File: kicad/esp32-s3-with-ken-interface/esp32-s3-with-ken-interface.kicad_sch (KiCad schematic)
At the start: 32 parts, among them J1 TYPE-C-31-M-12, Q1 UMH3N, SW1 TSC015A03526A, SW2 TSC015A03526A, SW3 TSC015A03526A, U1 CH340C, U2 AMS1117-3.3, U3 XDZ254-2-15-W-2.5-G1, U4 ESP32-S3-WROOM-1, U5 PM254-2-15-W-8.5

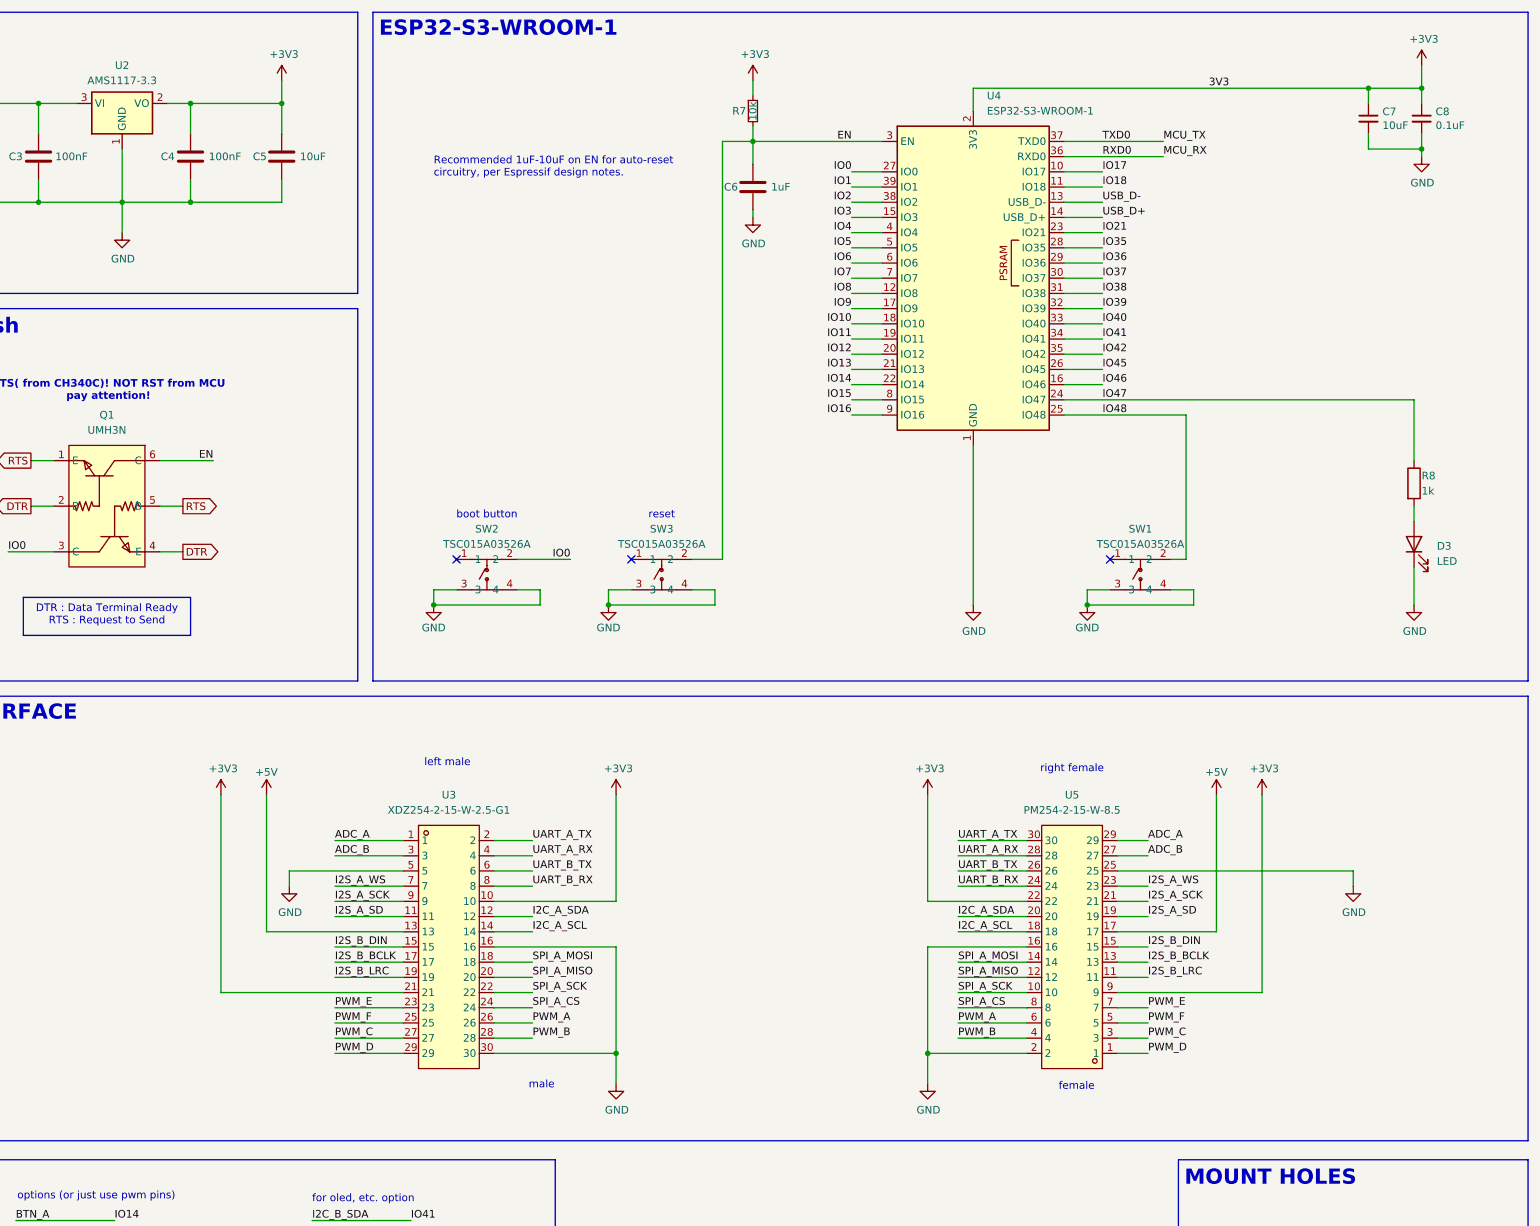
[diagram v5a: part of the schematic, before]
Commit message: add capacitor
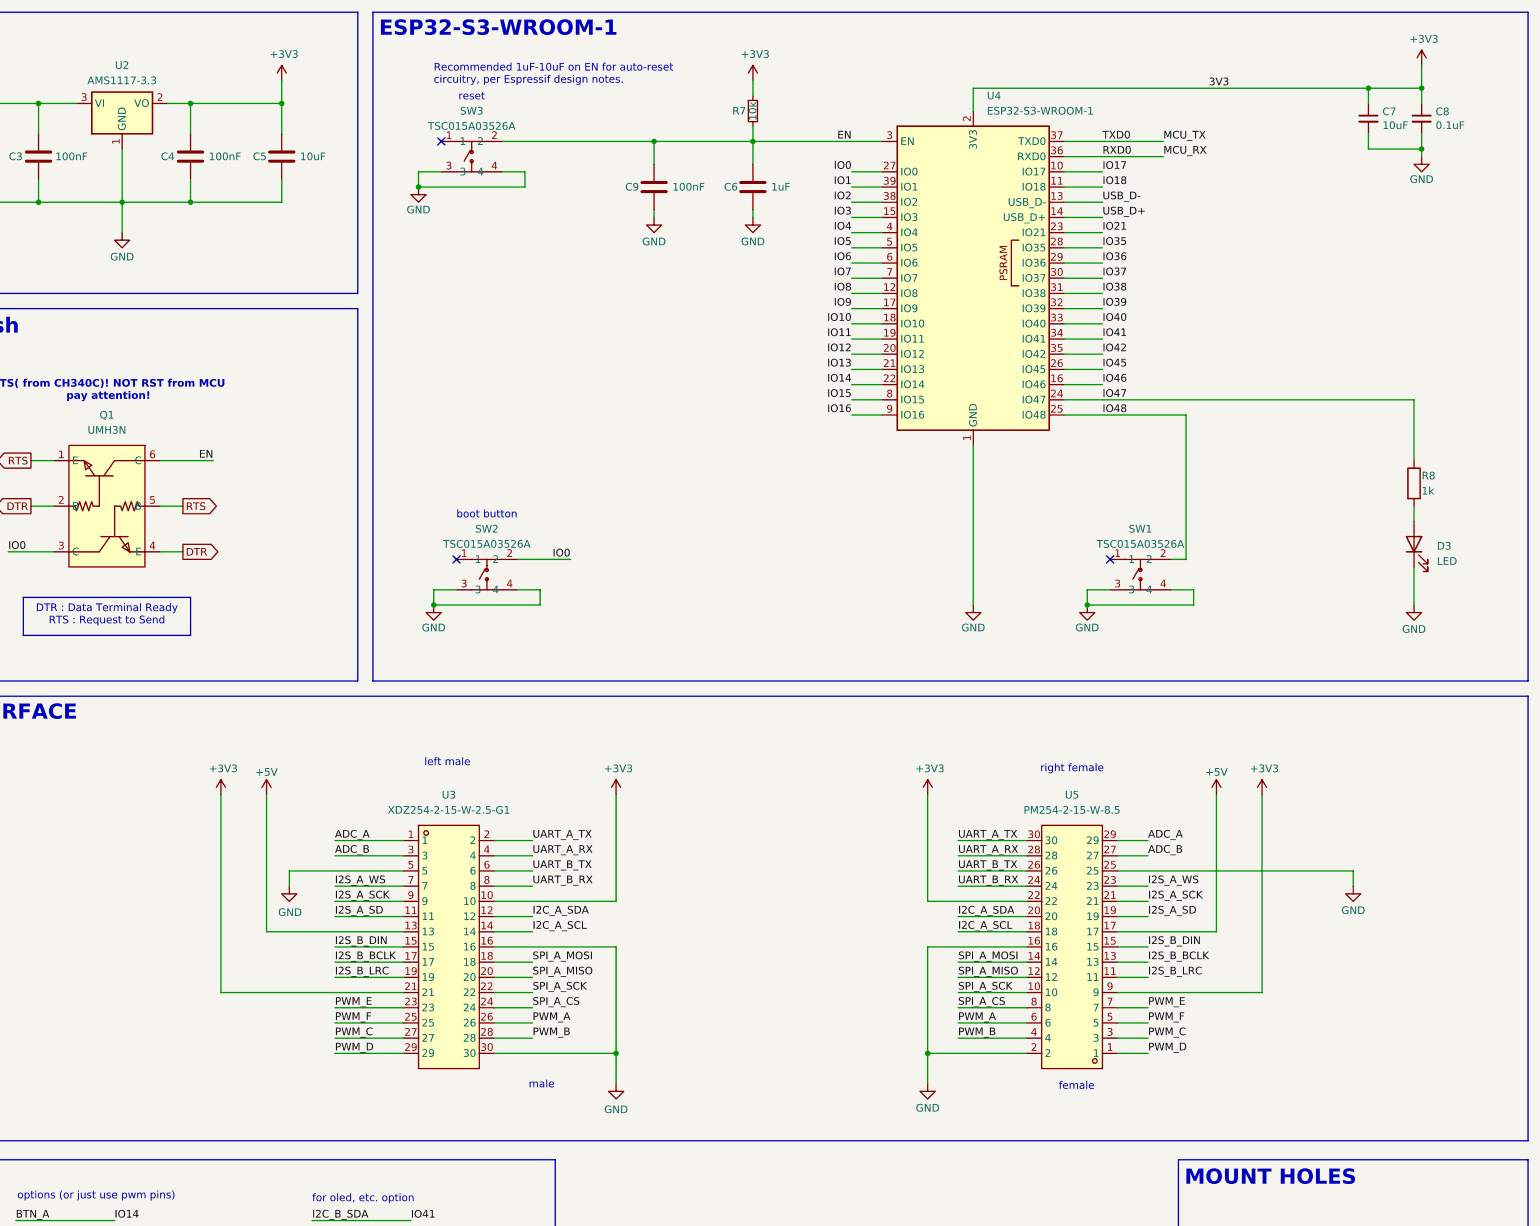
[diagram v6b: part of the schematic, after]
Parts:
- added C9: 100nF, Capacitor_SMD:C_0603_1608Metric_Pad1.08x0.95mm_HandSolder, symbol Device:C
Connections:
- net EN: now also C9.1
- net GND: now also C9.2
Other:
- moved on the sheet: SW3
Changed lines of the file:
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@@
 	(text "Recommended 1uF-10uF on EN for auto-reset\ncircuitry, per Espressif design notes."
 		(exclude_from_sim no)
-		(at 222.25 41.656 0)
+		(at 222.25 26.162 0)
 		(effects
 			(font
@@
 	(text "reset"
 		(exclude_from_sim no)
-		(at 260.35 98.044 0)
+		(at 228.6 28.194 0)
 		(effects
 			(font
@@
 	)
 	(junction
-		(at 251.46 113.03)
+		(at 219.71 43.18)
 		(diameter 0)
 		(color 0 0 0 0)
@@
 	)
 	(junction
+		(at 259.08 35.56)
+		(diameter 0)
+		(color 0 0 0 0)
+	)
+	(junction
 		(at 48.26 73.66)
 		(diameter 0)
@@
 	)
 	(no_connect
-		(at 255.27 105.41)
+		(at 223.52 35.56)
 	)
 	(no_connect
@@
 	(wire
 		(pts
-			(xy 269.24 113.03) (xy 251.46 113.03)
+			(xy 237.49 43.18) (xy 219.71 43.18)
+		)
+		(stroke
+			(width 0)
+			(type default)
+		)
+	)
+	(wire
+		(pts
+			(xy 259.08 46.99) (xy 259.08 48.26)
 		)
 		(stroke
@@
 	(wire
 		(pts
-			(xy 269.24 110.49) (xy 269.24 113.03)
+			(xy 237.49 40.64) (xy 237.49 43.18)
 		)
 		(stroke
@@
 	(wire
 		(pts
-			(xy 270.51 105.41) (xy 265.43 105.41)
+			(xy 233.68 35.56) (xy 259.08 35.56)
 		)
 		(stroke
@@
 	(wire
 		(pts
-			(xy 251.46 110.49) (xy 251.46 113.03)
+			(xy 219.71 40.64) (xy 219.71 43.18)
 		)
 		(stroke
@@
 	(wire
 		(pts
-			(xy 265.43 110.49) (xy 269.24 110.49)
+			(xy 233.68 40.64) (xy 237.49 40.64)
 		)
 		(stroke
@@
 	(wire
 		(pts
-			(xy 270.51 35.56) (xy 270.51 105.41)
+			(xy 181.61 29.21) (xy 181.61 34.29)
 		)
 		(stroke
@@
 	(wire
 		(pts
-			(xy 181.61 29.21) (xy 181.61 34.29)
+			(xy 259.08 35.56) (xy 275.59 35.56)
 		)
 		(stroke
@@
 	(wire
 		(pts
+			(xy 259.08 35.56) (xy 259.08 39.37)
+		)
+		(stroke
+			(width 0)
+			(type default)
+		)
+	)
+	(wire
+		(pts
 			(xy 252.73 170.18) (xy 252.73 187.96)
 		)
@@
 	(wire
 		(pts
-			(xy 275.59 35.56) (xy 270.51 35.56)
-		)
-		(stroke
-			(width 0)
-			(type default)
-		)
-	)
-	(wire
-		(pts
 			(xy 27.94 190.5) (xy 44.45 190.5)
 		)
@@
 	(wire
 		(pts
-			(xy 255.27 110.49) (xy 251.46 110.49)
+			(xy 223.52 40.64) (xy 219.71 40.64)
 		)
 		(stroke
@@
 		)
 		(property "Value" "GND"
-			(at 275.717 52.6542 0)
+			(at 275.59 52.324 0)
 			(show_name no)
 			(do_not_autoplace no)
@@
 	)
 	(symbol
+		(lib_id "power:GND")
+		(at 259.08 48.26 0)
+		(unit 1)
+		(body_style 1)
+		(exclude_from_sim no)
+		(in_bom yes)
+		(on_board yes)
+		(in_pos_files yes)
+		(dnp no)
+		(property "Reference" "#PWR030"
+			(at 259.08 54.61 0)
+			(hide yes)
+			(show_name no)
+			(do_not_autoplace no)
+			(effects
+				(font
+					(size 1.27 1.27)
+				)
+			)
+		)
+		(property "Value" "GND"
+			(at 259.08 52.324 0)
+			(show_name no)
+			(do_not_autoplace no)
+			(effects
+				(font
+					(size 1.27 1.27)
+				)
+			)
+		)
+		(property "Footprint" ""
+			(at 259.08 48.26 0)
+			(hide yes)
+			(show_name no)
+			(do_not_autoplace no)
+			(effects
+				(font
+					(size 1.27 1.27)
+				)
+			)
+		)
+		(property "Datasheet" ""
+			(at 259.08 48.26 0)
+			(hide yes)
+			(show_name no)
+			(do_not_autoplace no)
+			(effects
+				(font
+					(size 1.27 1.27)
+				)
+			)
+		)
+		(property "Description" ""
+			(at 259.08 48.26 0)
+			(hide yes)
+			(show_name no)
+			(do_not_autoplace no)
+			(effects
+				(font
+					(size 1.27 1.27)
+				)
+			)
+		)
+		(pin "1"
+		)
+		(instances
+			(project "esp32-s3-with-ken-interface"
+				(path "/5edcefbe-9766-42c8-9529-28d0ec865573"
+					(reference "#PWR030")
+					(unit 1)
+				)
+			)
+		)
+	)
+	(symbol
 		(lib_id "power:+3.3V")
 		(at 100.33 71.12 0)
@@
 		)
 		(property "Value" "GND"
-			(at 387.477 42.4942 0)
+			(at 387.35 41.91 0)
 			(show_name no)
 			(do_not_autoplace no)
@@
 		)
 		(property "Value" "GND"
-			(at 312.547 117.4242 0)
+			(at 312.42 116.84 0)
 			(show_name no)
 			(do_not_autoplace no)
@@
 	(symbol
 		(lib_id "TSC015A03526A:TSC015A03526A")
-		(at 260.35 107.95 0)
+		(at 228.6 38.1 0)
 		(unit 1)
 		(body_style 1)
@@
 		(fields_autoplaced yes)
 		(property "Reference" "SW3"
-			(at 260.35 100.33 0)
+			(at 228.6 30.48 0)
 			(show_name no)
 			(do_not_autoplace no)
@@
 		)
 		(property "Value" "TSC015A03526A"
-			(at 260.35 102.87 0)
+			(at 228.6 33.02 0)
 			(show_name no)
 			(do_not_autoplace no)
@@
 		)
 		(property "Footprint" "TSC015A03526A:SW-SMD_4P-L4.5-W4.5-P3.00-LS6.8"
-			(at 260.35 118.11 0)
+			(at 228.6 48.26 0)
 			(hide yes)
 			(show_name no)
@@
 		)
 		(property "Datasheet" ""
-			(at 260.35 107.95 0)
+			(at 228.6 38.1 0)
 			(hide yes)
 			(show_name no)
@@
 		)
 		(property "Description" ""
-			(at 260.35 107.95 0)
+			(at 228.6 38.1 0)
 			(hide yes)
 			(show_name no)
@@
 		)
 		(property "LCSC Part" "C2888900"
-			(at 260.35 120.65 0)
+			(at 228.6 50.8 0)
 			(hide yes)
 			(show_name no)
@@
 		)
 		(property "Value" "GND"
-			(at 376.047 164.4142 0)
+			(at 375.92 164.084 0)
 			(show_name no)
 			(do_not_autoplace no)
@@
 		)
 		(property "Value" "GND"
-			(at 170.307 55.1942 0)
+			(at 170.18 54.864 0)
 			(show_name no)
 			(do_not_autoplace no)
@@
 		)
 		(property "Value" "GND"
-			(at 386.207 117.4242 0)
+			(at 386.08 117.094 0)
 			(show_name no)
 			(do_not_autoplace no)
@@
 		)
 		(property "Value" "GND"
-			(at 304.927 197.4342 0)
+			(at 304.8 197.104 0)
 			(show_name no)
 			(do_not_autoplace no)
@@
 	(symbol
 		(lib_id "power:GND")
-		(at 251.46 113.03 0)
+		(at 219.71 43.18 0)
 		(unit 1)
 		(body_style 1)
@@
 		(dnp no)
 		(property "Reference" "#PWR029"
-			(at 251.46 119.38 0)
+			(at 219.71 49.53 0)
 			(hide yes)
 			(show_name no)
@@
 		)
 		(property "Value" "GND"
-			(at 251.46 116.84 0)
+			(at 219.71 46.99 0)
 			(show_name no)
 			(do_not_autoplace no)
@@
 		)
 		(property "Footprint" ""
-			(at 251.46 113.03 0)
+			(at 219.71 43.18 0)
 			(hide yes)
 			(show_name no)
@@
 		)
 		(property "Datasheet" ""
-			(at 251.46 113.03 0)
+			(at 219.71 43.18 0)
 			(hide yes)
 			(show_name no)
@@
 		)
 		(property "Description" ""
-			(at 251.46 113.03 0)
+			(at 219.71 43.18 0)
 			(hide yes)
 			(show_name no)
@@
 		)
 		(property "Value" "GND"
-			(at 252.857 197.4342 0)
+			(at 252.73 197.358 0)
 			(show_name no)
 			(do_not_autoplace no)
@@
 					(unit 1)
 				)
+			)
+		)
+	)
+	(symbol
+		(lib_id "Device:C")
+		(at 259.08 43.18 0)
+		(unit 1)
+		(body_style 1)
+		(exclude_from_sim no)
+		(in_bom yes)
+		(on_board yes)
+		(in_pos_files yes)
+		(dnp no)
+		(property "Reference" "C9"
+			(at 254.254 43.18 0)
+			(show_name no)
+			(do_not_autoplace no)
+			(effects
+				(font
+					(size 1.27 1.27)
+				)
+				(justify left)
+			)
+		)
+		(property "Value" "100nF"
+			(at 262.128 43.18 0)
+			(show_name no)
+			(do_not_autoplace no)
+			(effects
+				(font
+					(size 1.27 1.27)
+				)
+				(justify left)
+			)
+		)
+		(property "Footprint" "Capacitor_SMD:C_0603_1608Metric_Pad1.08x0.95mm_HandSolder"
+			(at 260.0452 46.99 0)
+			(hide yes)
+			(show_name no)
+			(do_not_autoplace no)
+			(effects
+				(font
+					(size 1.27 1.27)
+				)
+			)
+		)
+		(property "Datasheet" ""
+			(at 259.08 43.18 0)
+			(hide yes)
+			(show_name no)
+			(do_not_autoplace no)
+			(effects
+				(font
+					(size 1.27 1.27)
+				)
+			)
+		)
+		(property "Description" "Unpolarized capacitor"
+			(at 259.08 43.18 0)
+			(hide yes)
+			(show_name no)
+			(do_not_autoplace no)
+			(effects
+				(font
+					(size 1.27 1.27)
+				)
+			)
+		)
+		(pin "1"
+		)
+		(pin "2"
+		)
+		(instances
+			(project "esp32-s3-with-ken-interface"
+				(path "/5edcefbe-9766-42c8-9529-28d0ec865573"
+					(reference "C9")
+					(unit 1)
+				)
